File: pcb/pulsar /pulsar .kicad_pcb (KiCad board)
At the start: 16 copper layers, 292 x 102 mm, 414 parts, among them J1 GX-C-065 USB-C, J2 FPC-10p 0.5mm, U1 XC7A200T-2FBG484I, U10 PRTR5V0U2X, U3 W25Q128JVSIQ, U9 IS61WV102416BLL, Y1 50MHz_XTAL, Y2 48MHz_XTAL

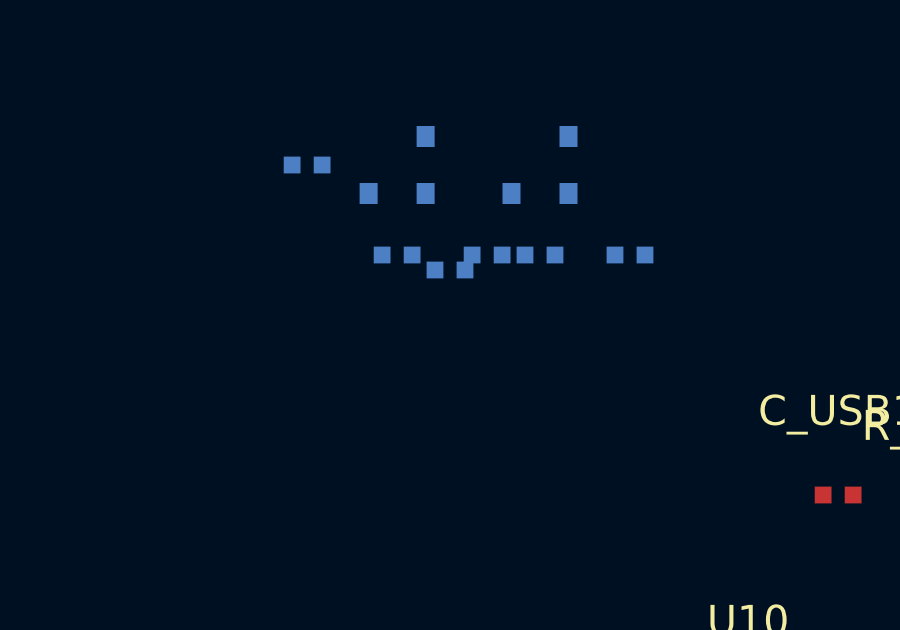
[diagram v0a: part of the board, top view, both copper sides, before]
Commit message: fix: separation of overlapped components
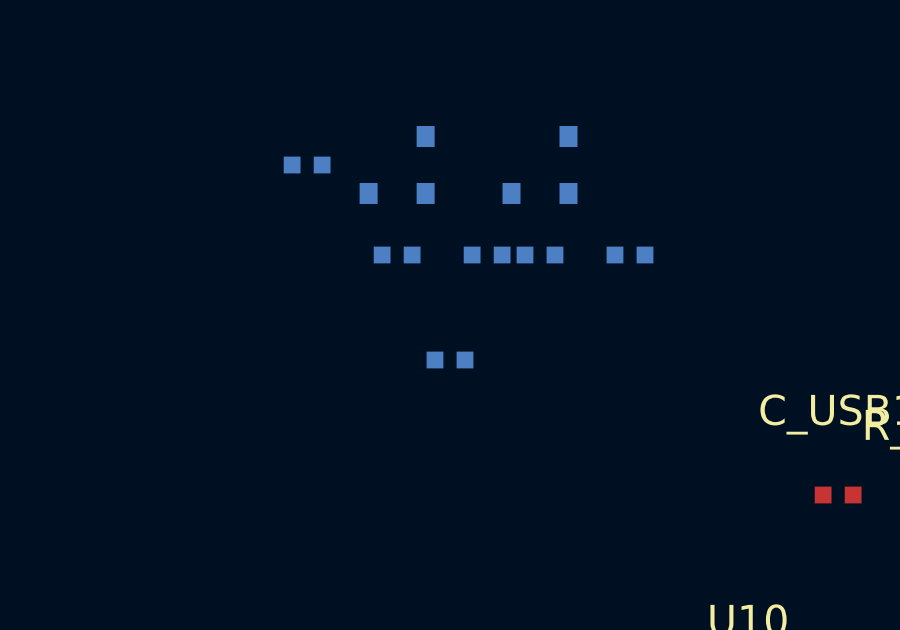
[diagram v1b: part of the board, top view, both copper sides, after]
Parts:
- moved CB_H27 3.00 mm to (262.1, 39.5)
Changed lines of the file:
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@@
 	(footprint "Device:C_0402"
 		(layer "B.Cu")
-		(at 262.0625 36.5)
+		(at 262.0625 39.5)
 		(property "Reference" "CB_H27"
 			(at 0 -2.8 0)
